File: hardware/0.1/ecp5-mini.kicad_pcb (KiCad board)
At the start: 4 copper layers, 52 x 27 mm, 105 parts, among them J1 Micro_SD_Card, J2 JTAG, J3 S7 Mini, J4 S7 Mini, J5 USB_C_Receptacle_USB2.0, Q1 BSS138, Q2 BSS138, Q3 BSS138, Q4 BSS138, SW1 KMR2, U1 ECP5U_12_CABGA256, U2 TLV73325PDBV, U3 TLV62568DBV, U4 USBLC6-2P6, U5 TLV62568DBV, U6 W25Q128JVPIQ, U7 S27KL0641, X1 DSC6101CI2A-016

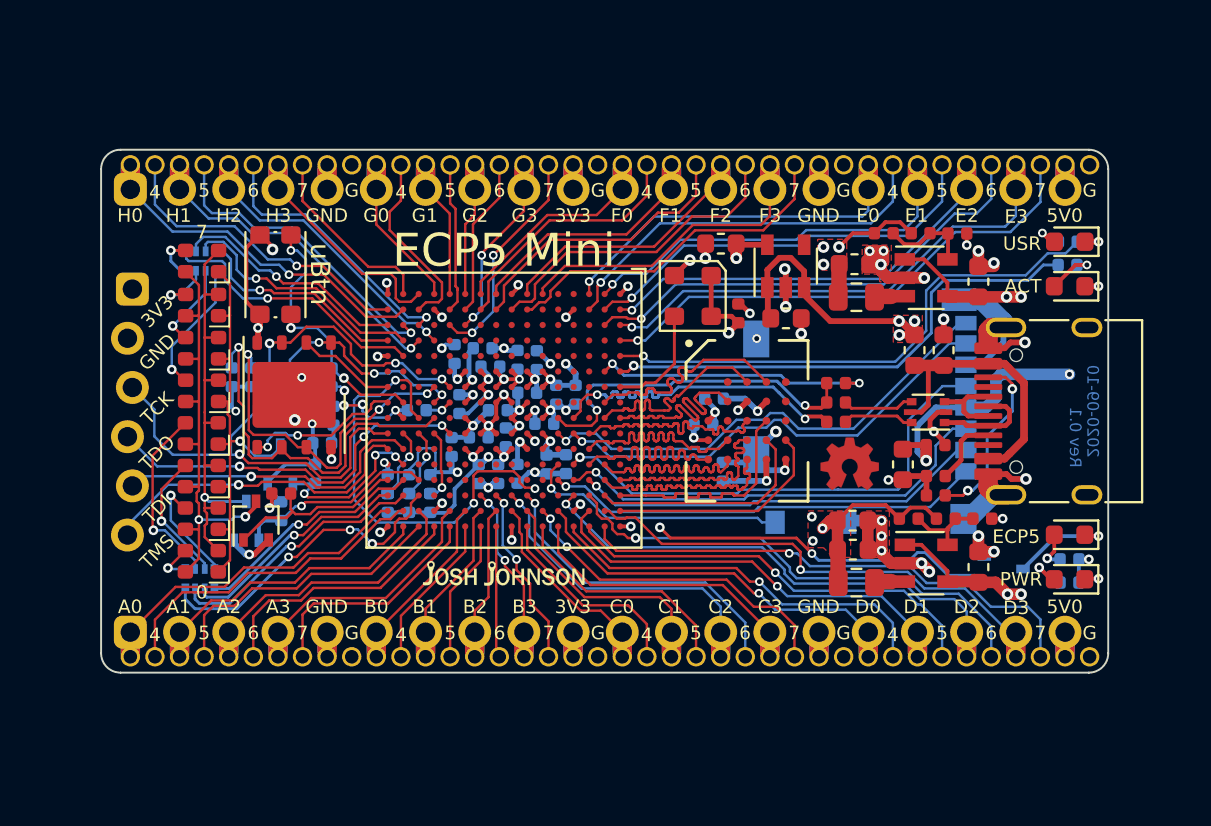
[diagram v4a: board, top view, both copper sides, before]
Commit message: add fiducals
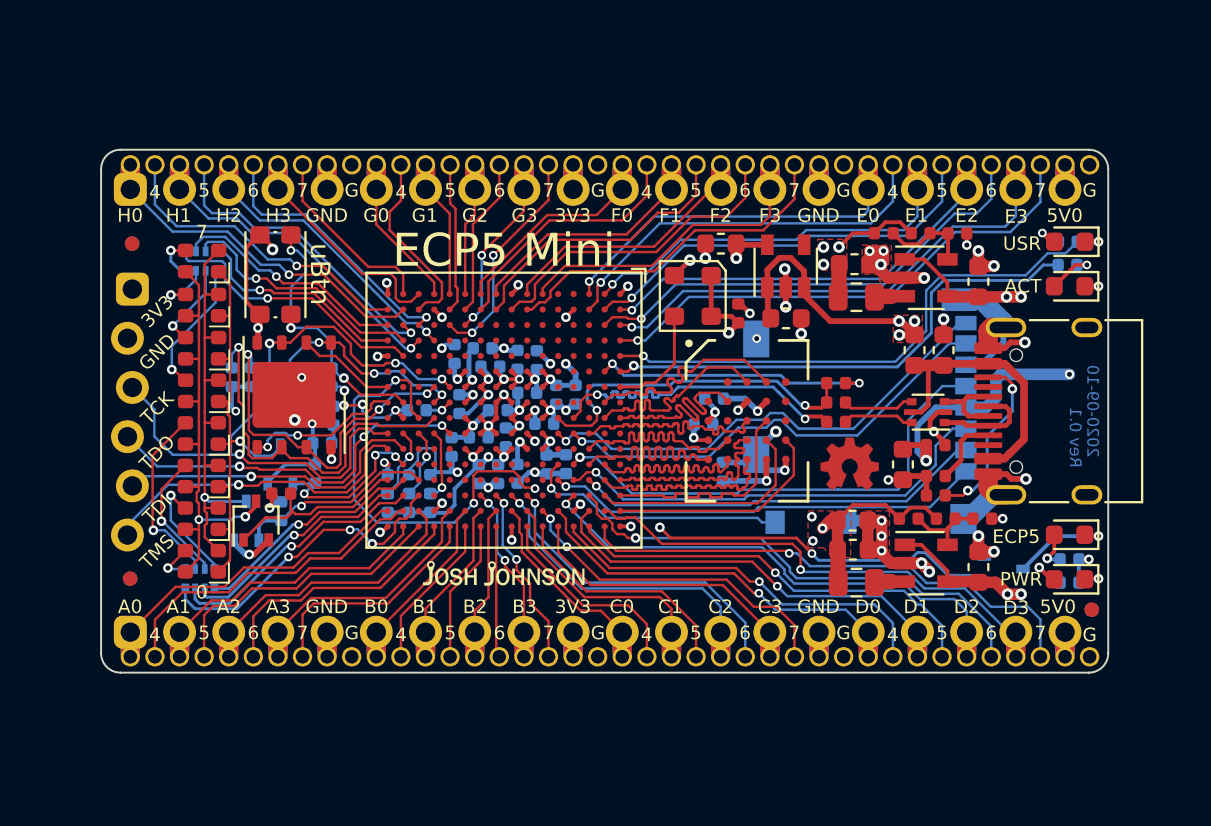
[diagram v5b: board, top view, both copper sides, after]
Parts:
- added FID1: Fiducial, Fiducial:Fiducial_0.75mm_Mask1.5mm, F.Cu at (147.3, 105.2)
- added FID2: Fiducial, Fiducial:Fiducial_0.75mm_Mask1.5mm, B.Cu at (97.8, 86.3)
- added FID3: Fiducial, Fiducial:Fiducial_0.75mm_Mask1.5mm, B.Cu at (147.3, 105.2)
- added FID4: Fiducial, Fiducial:Fiducial_0.75mm_Mask1.5mm, B.Cu at (97.7, 103.6)
- added FID5: Fiducial, Fiducial:Fiducial_0.75mm_Mask1.5mm, F.Cu at (97.8, 86.3)
- added FID6: Fiducial, Fiducial:Fiducial_0.75mm_Mask1.5mm, F.Cu at (97.7, 103.6)
- U6: value W25Q128JVPIQ -> W25Q128JVPIM
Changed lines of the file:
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@@
     )
   )
+  (module "Fiducial:Fiducial_0.75mm_Mask1.5mm" (layer "F.Cu")
+    (at 97.8 86.3)
+    (descr "Circular Fiducial, 0.75mm bare copper, 1.5mm soldermask opening (Level B)")
+    (tags "fiducial")
+    (property "Sheet file" "/mnt/530683E96DD773A1/Dropbox/Projects/ecp5-mini/hardware/0.1/ecp5-mini.kicad_sch")
+    (property "Sheet name" "")
+    (attr smd)
+    (fp_text reference "FID5" (at 0 -2) (layer "F.SilkS") hide
+      (effects (font (size 1 1) (thickness 0.15)))
+    )
+    (fp_text value "Fiducial" (at 0 2) (layer "F.Fab")
+      (effects (font (size 1 1) (thickness 0.15)))
+    )
+    (fp_text user "${REFERENCE}" (at 0 0) (layer "F.Fab") hide
+      (effects (font (size 0.3 0.3) (thickness 0.05)))
+    )
+    (fp_circle (center 0 0) (end 1 0) (layer "F.CrtYd") (width 0.05))
+    (fp_circle (center 0 0) (end 0.75 0) (layer "F.Fab") (width 0.1))
+    (pad "" smd circle (at 0 0) (size 0.75 0.75) (layers "F.Cu" "F.Mask")
+      (solder_mask_margin 0.375) (clearance 0.375))
+  )
   (module "Resistor_SMD:R_0402_1005Metric" (layer "F.Cu")
     (at 139.3 98.3 180)
@@
     )
   )
+  (module "Fiducial:Fiducial_0.75mm_Mask1.5mm" (layer "F.Cu")
+    (at 147.35 105.2)
+    (descr "Circular Fiducial, 0.75mm bare copper, 1.5mm soldermask opening (Level B)")
+    (tags "fiducial")
+    (property "Sheet file" "/mnt/530683E96DD773A1/Dropbox/Projects/ecp5-mini/hardware/0.1/ecp5-mini.kicad_sch")
+    (property "Sheet name" "")
+    (attr smd)
+    (fp_text reference "FID1" (at 0 -2) (layer "F.SilkS") hide
+      (effects (font (size 1 1) (thickness 0.15)))
+    )
+    (fp_text value "Fiducial" (at 0 2) (layer "F.Fab")
+      (effects (font (size 1 1) (thickness 0.15)))
+    )
+    (fp_text user "${REFERENCE}" (at 0 0) (layer "F.Fab") hide
+      (effects (font (size 0.3 0.3) (thickness 0.05)))
+    )
+    (fp_circle (center 0 0) (end 1 0) (layer "F.CrtYd") (width 0.05))
+    (fp_circle (center 0 0) (end 0.75 0) (layer "F.Fab") (width 0.1))
+    (pad "" smd circle (at 0 0) (size 0.75 0.75) (layers "F.Cu" "F.Mask")
+      (solder_mask_margin 0.375) (clearance 0.375))
+  )
   (module "josh-led:LED_TRI_2020" (layer "F.Cu")
     (at 101.415 89.474 180)
@@
     (descr "Oscilator suits Microchip DSC 6xxx series")
     (property "MPN" "DSC6101CI2A-016.0000 ")
+    (property "Manufacturer" "Microchip")
     (property "Mouser" "579-101CI2A0160000 ")
     (property "Sheet file" "/mnt/530683E96DD773A1/Dropbox/Projects/ecp5-mini/hardware/0.1/ecp5-mini.kicad_sch")
@@
     )
   )
+  (module "Fiducial:Fiducial_0.75mm_Mask1.5mm" (layer "F.Cu")
+    (at 97.7 103.6)
+    (descr "Circular Fiducial, 0.75mm bare copper, 1.5mm soldermask opening (Level B)")
+    (tags "fiducial")
+    (property "Sheet file" "/mnt/530683E96DD773A1/Dropbox/Projects/ecp5-mini/hardware/0.1/ecp5-mini.kicad_sch")
+    (property "Sheet name" "")
+    (attr smd)
+    (fp_text reference "FID6" (at 0 -2) (layer "F.SilkS") hide
+      (effects (font (size 1 1) (thickness 0.15)))
+    )
+    (fp_text value "Fiducial" (at 0 2) (layer "F.Fab")
+      (effects (font (size 1 1) (thickness 0.15)))
+    )
+    (fp_text user "${REFERENCE}" (at 0 0) (layer "F.Fab") hide
+      (effects (font (size 0.3 0.3) (thickness 0.05)))
+    )
+    (fp_circle (center 0 0) (end 1 0) (layer "F.CrtYd") (width 0.05))
+    (fp_circle (center 0 0) (end 0.75 0) (layer "F.Fab") (width 0.1))
+    (pad "" smd circle (at 0 0) (size 0.75 0.75) (layers "F.Cu" "F.Mask")
+      (solder_mask_margin 0.375) (clearance 0.375))
+  )
   (module "Capacitor_SMD:C_0402_1005Metric" (layer "F.Cu")
     (at 129.1 89.9 90)
@@
       (effects (font (size 1 1) (thickness 0.15)))
     )
-    (fp_text value "W25Q128JVPIQ" (at 0 3.45 -90) (layer "F.Fab")
+    (fp_text value "W25Q128JVPIM" (at 0 3.45 -90) (layer "F.Fab")
       (effects (font (size 1 1) (thickness 0.15)))
     )
@@
     )
   )
+  (module "Fiducial:Fiducial_0.75mm_Mask1.5mm" (layer "B.Cu")
+    (at 97.8 86.3 180)
+    (descr "Circular Fiducial, 0.75mm bare copper, 1.5mm soldermask opening (Level B)")
+    (tags "fiducial")
+    (property "Sheet file" "/mnt/530683E96DD773A1/Dropbox/Projects/ecp5-mini/hardware/0.1/ecp5-mini.kicad_sch")
+    (property "Sheet name" "")
+    (attr smd)
+    (fp_text reference "FID2" (at 0 2) (layer "B.SilkS") hide
+      (effects (font (size 1 1) (thickness 0.15)) (justify mirror))
+    )
+    (fp_text value "Fiducial" (at 0 -2) (layer "B.Fab")
+      (effects (font (size 1 1) (thickness 0.15)) (justify mirror))
+    )
+    (fp_text user "${REFERENCE}" (at 0 0) (layer "B.Fab") hide
+      (effects (font (size 0.3 0.3) (thickness 0.05)) (justify mirror))
+    )
+    (fp_circle (center 0 0) (end 1 0) (layer "B.CrtYd") (width 0.05))
+    (fp_circle (center 0 0) (end 0.75 0) (layer "B.Fab") (width 0.1))
+    (pad "" smd circle (at 0 0 180) (size 0.75 0.75) (layers "B.Cu" "B.Mask")
+      (solder_mask_margin 0.375) (clearance 0.375))
+  )
   (module "Resistor_SMD:R_0402_1005Metric" (layer "B.Cu")
     (at 104.95 93.2 90)
@@
     )
   )
+  (module "Fiducial:Fiducial_0.75mm_Mask1.5mm" (layer "B.Cu")
+    (at 147.35 105.2 180)
+    (descr "Circular Fiducial, 0.75mm bare copper, 1.5mm soldermask opening (Level B)")
+    (tags "fiducial")
+    (property "Sheet file" "/mnt/530683E96DD773A1/Dropbox/Projects/ecp5-mini/hardware/0.1/ecp5-mini.kicad_sch")
+    (property "Sheet name" "")
+    (attr smd)
+    (fp_text reference "FID3" (at 0 2) (layer "B.SilkS") hide
+      (effects (font (size 1 1) (thickness 0.15)) (justify mirror))
+    )
+    (fp_text value "Fiducial" (at 0 -2) (layer "B.Fab")
+      (effects (font (size 1 1) (thickness 0.15)) (justify mirror))
+    )
+    (fp_text user "${REFERENCE}" (at 0 0) (layer "B.Fab") hide
+      (effects (font (size 0.3 0.3) (thickness 0.05)) (justify mirror))
+    )
+    (fp_circle (center 0 0) (end 1 0) (layer "B.CrtYd") (width 0.05))
+    (fp_circle (center 0 0) (end 0.75 0) (layer "B.Fab") (width 0.1))
+    (pad "" smd circle (at 0 0 180) (size 0.75 0.75) (layers "B.Cu" "B.Mask")
+      (solder_mask_margin 0.375) (clearance 0.375))
+  )
   (module "Capacitor_SMD:C_0402_1005Metric" (layer "B.Cu")
     (at 116.685 94.9)
@@
     )
   )
+  (module "Fiducial:Fiducial_0.75mm_Mask1.5mm" (layer "B.Cu")
+    (at 97.7 103.6 180)
+    (descr "Circular Fiducial, 0.75mm bare copper, 1.5mm soldermask opening (Level B)")
+    (tags "fiducial")
+    (property "Sheet file" "/mnt/530683E96DD773A1/Dropbox/Projects/ecp5-mini/hardware/0.1/ecp5-mini.kicad_sch")
+    (property "Sheet name" "")
+    (attr smd)
+    (fp_text reference "FID4" (at 0 2) (layer "B.SilkS") hide
+      (effects (font (size 1 1) (thickness 0.15)) (justify mirror))
+    )
+    (fp_text value "Fiducial" (at 0 -2) (layer "B.Fab")
+      (effects (font (size 1 1) (thickness 0.15)) (justify mirror))
+    )
+    (fp_text user "${REFERENCE}" (at 0 0) (layer "B.Fab") hide
+      (effects (font (size 0.3 0.3) (thickness 0.05)) (justify mirror))
+    )
+    (fp_circle (center 0 0) (end 1 0) (layer "B.CrtYd") (width 0.05))
+    (fp_circle (center 0 0) (end 0.75 0) (layer "B.Fab") (width 0.1))
+    (pad "" smd circle (at 0 0 180) (size 0.75 0.75) (layers "B.Cu" "B.Mask")
+      (solder_mask_margin 0.375) (clearance 0.375))
+  )
   (module "Capacitor_SMD:C_0402_1005Metric" (layer "B.Cu")
     (at 107.615 96.6 180)
@@
     (effects (font (size 0.6 0.6) (thickness 0.127)) (justify mirror))
   )
-  (gr_text "G" (at 147.24 106.4) (layer "F.SilkS")
+  (gr_text "G" (at 147.24 106.5) (layer "F.SilkS")
     (effects (font (size 0.7 0.7) (thickness 0.12)))
   )
@@
     (effects (font (size 0.7 0.7) (thickness 0.12)))
   )
-  (gr_text "5V0" (at 145.95 105.05) (layer "F.SilkS")
+  (gr_text "5V0" (at 145.6 105.05) (layer "F.SilkS")
     (effects (font (size 0.7 0.7) (thickness 0.12)))
   )
@@
   (segment (start 135.81 84.59) (end 135.5 84.9) (width 0.127) (layer "B.Cu") (net 60))
   (segment (start 103.7 86.5) (end 104.35 85.85) (width 0.2) (layer "F.Cu") (net 61))
+  (segment (start 142.275 87.475) (end 142.3 87.45) (width 0.6) (layer "F.Cu") (net 61))
   (segment (start 117.8 94.9) (end 117.4 95.3) (width 0.2) (layer "F.Cu") (net 61))
   (segment (start 135.897636 86.675) (end 135.885136 86.6875) (width 0.6) (layer "F.Cu") (net 61))
@@
   (segment (start 116.6 94.49192) (end 116.999999 94.091921) (width 0.2) (layer "F.Cu") (net 61))
   (segment (start 117.4 95.3) (end 117.8 95.7) (width 0.2) (layer "F.Cu") (net 61))
-  (segment (start 141.497636 87.475) (end 142.297636 87.475) (width 0.6) (layer "F.Cu") (net 61))
   (segment (start 131.551499 97.949991) (end 131.50149 98) (width 0.3) (layer "F.Cu") (net 61))
   (segment (start 146.9875 88.5) (end 147.7 88.5) (width 0.3) (layer "F.Cu") (net 61))
@@
   (segment (start 125.8 87.95) (end 126.6 87.15) (width 0.25) (layer "F.Cu") (net 61))
   (segment (start 132.35 90.15625) (end 132.35 90.95) (width 0.3) (layer "F.Cu") (net 61))
+  (segment (start 141.497636 87.475) (end 142.275 87.475) (width 0.6) (layer "F.Cu") (net 61))
   (segment (start 116.6 95.3) (end 116.6 94.5) (width 0.2) (layer "F.Cu") (net 61))
   (segment (start 136.597636 86.675) (end 136.597636 87.241755) (width 0.6) (layer "F.Cu") (net 61))
@@
   (via (at 106.2 95.4) (size 0.6) (drill 0.3) (layers "F.Cu" "B.Cu") (net 61))
   (via (at 106.561897 93.205247) (size 0.45) (drill 0.25) (layers "F.Cu" "B.Cu") (net 61))
-  (via (at 142.297636 87.3) (size 0.6) (drill 0.3) (layers "F.Cu" "B.Cu") (net 61))
+  (via (at 142.297636 87.45) (size 0.6) (drill 0.3) (layers "F.Cu" "B.Cu") (net 61))
   (via (at 117.8 94.9) (size 0.5) (drill 0.25) (layers "F.Cu" "B.Cu") (net 61))
   (via (at 110.949992 88.322256) (size 0.5) (drill 0.25) (layers "F.Cu" "B.Cu") (net 61))

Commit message: set clearances to a more reasonable number
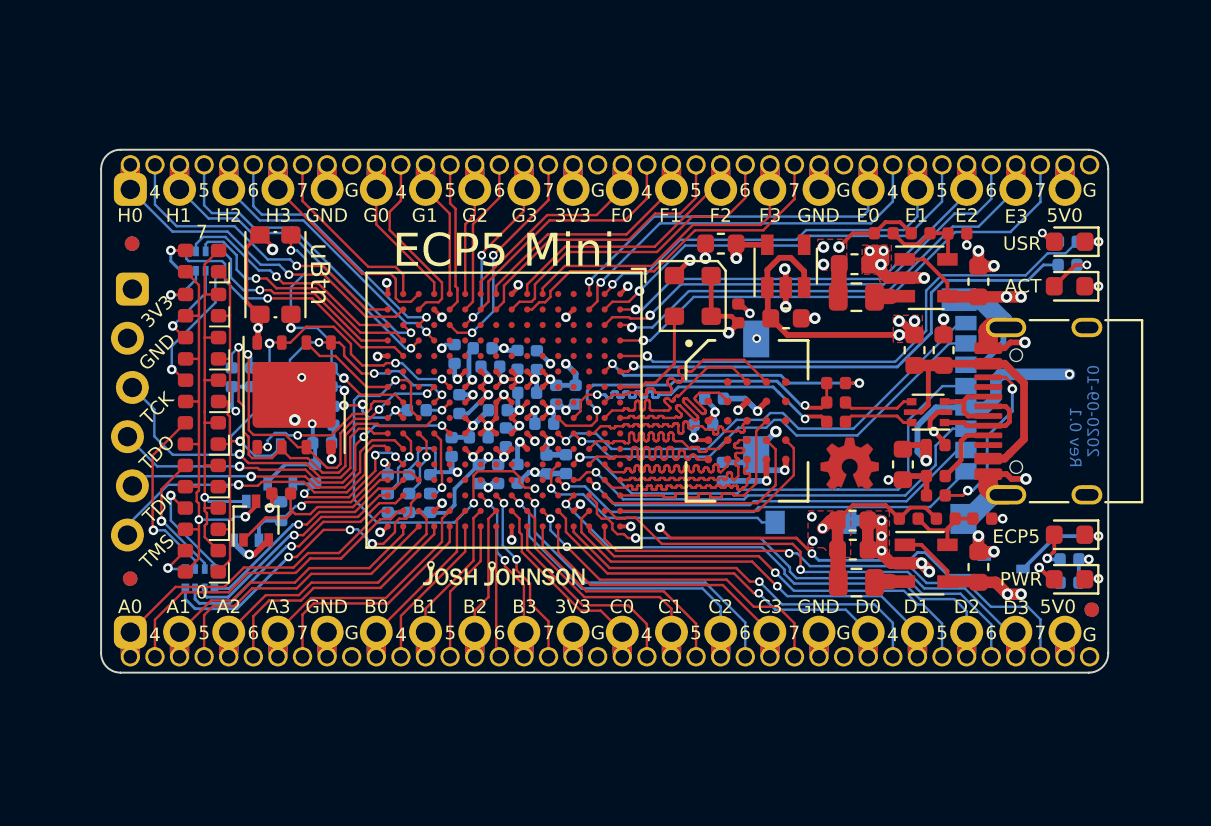
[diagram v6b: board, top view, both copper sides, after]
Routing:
- net +5V: track 71.6 -> 73.8 mm
- net /PORT_E3: track 24.2 -> 23.4 mm

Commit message: quad pmod looks good
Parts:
- U6: value W25Q128JVPIM -> W25Q128JVPIQ
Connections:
- net /FPGA_OK renamed /LED_ACT
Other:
- board text added: "2020-09-13"
- board text removed: "2020-09-10"
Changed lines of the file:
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@@
       (usegerberextensions true)
       (usegerberattributes false)
-      (usegerberadvancedattributes true)
+      (usegerberadvancedattributes false)
       (creategerberjobfile false)
       (svguseinch false)
@@
   (net 229 "/PORT_H0")
   (net 230 "/LED_USR")
-  (net 231 "/FPGA_OK")
+  (net 231 "/LED_ACT")
   (net 232 "Net-(U1-PadR7)")
   (net 233 "Net-(U1-PadR6)")
@@
     (descr "Circular Fiducial, 0.75mm bare copper, 1.5mm soldermask opening (Level B)")
     (tags "fiducial")
+    (property "DNP" "DNP")
     (property "Sheet file" "/mnt/530683E96DD773A1/Dropbox/Projects/ecp5-mini/hardware/0.1/ecp5-mini.kicad_sch")
     (property "Sheet name" "")
@@
     (descr "Circular Fiducial, 0.75mm bare copper, 1.5mm soldermask opening (Level B)")
     (tags "fiducial")
+    (property "DNP" "DNP")
     (property "Sheet file" "/mnt/530683E96DD773A1/Dropbox/Projects/ecp5-mini/hardware/0.1/ecp5-mini.kicad_sch")
     (property "Sheet name" "")
@@
       (net 230 "/LED_USR") (pinfunction "PT18A/+"))
     (pad "A6" smd circle (at -2 -6 270) (size 0.32 0.32) (layers "F.Cu" "F.Paste" "F.Mask")
-      (net 231 "/FPGA_OK") (pinfunction "PT18B/-"))
+      (net 231 "/LED_ACT") (pinfunction "PT18B/-"))
     (pad "A7" smd circle (at -1.2 -6 270) (size 0.32 0.32) (layers "F.Cu" "F.Paste" "F.Mask")
       (net 167 "/CLK_16MHZ") (pinfunction "PT29A/+/PCLKT0_0"))
@@
     (descr "Circular Fiducial, 0.75mm bare copper, 1.5mm soldermask opening (Level B)")
     (tags "fiducial")
+    (property "DNP" "DNP")
     (property "Sheet file" "/mnt/530683E96DD773A1/Dropbox/Projects/ecp5-mini/hardware/0.1/ecp5-mini.kicad_sch")
     (property "Sheet name" "")
@@
     (descr "WSON, 8 Pin (http://www.winbond.com/resource-files/w25q32jv%20revg%2003272018%20plus.pdf (page 68)), generated with kicad-footprint-generator ipc_dfn_qfn_generator.py")
     (tags "WSON DFN_QFN")
-    (property "MPN" "W25Q128JVPIM")
+    (property "MPN" "W25Q128JVPIQ")
     (property "Manufacturer" "Winbond")
-    (property "Mouser" "454-W25Q128JVPIM")
+    (property "Mouser" "454-W25Q128JVPIQ")
     (property "Sheet file" "fpga-config.kicad_sch")
     (property "Sheet name" "FPGA Config")
@@
       (effects (font (size 1 1) (thickness 0.15)))
     )
-    (fp_text value "W25Q128JVPIM" (at 0 3.45 -90) (layer "F.Fab")
+    (fp_text value "W25Q128JVPIQ" (at 0 3.45 -90) (layer "F.Fab")
       (effects (font (size 1 1) (thickness 0.15)))
     )
@@
     (descr "Circular Fiducial, 0.75mm bare copper, 1.5mm soldermask opening (Level B)")
     (tags "fiducial")
+    (property "DNP" "DNP")
     (property "Sheet file" "/mnt/530683E96DD773A1/Dropbox/Projects/ecp5-mini/hardware/0.1/ecp5-mini.kicad_sch")
     (property "Sheet name" "")
@@
     (descr "Circular Fiducial, 0.75mm bare copper, 1.5mm soldermask opening (Level B)")
     (tags "fiducial")
+    (property "DNP" "DNP")
     (property "Sheet file" "/mnt/530683E96DD773A1/Dropbox/Projects/ecp5-mini/hardware/0.1/ecp5-mini.kicad_sch")
     (property "Sheet name" "")
@@
     (descr "Circular Fiducial, 0.75mm bare copper, 1.5mm soldermask opening (Level B)")
     (tags "fiducial")
+    (property "DNP" "DNP")
     (property "Sheet file" "/mnt/530683E96DD773A1/Dropbox/Projects/ecp5-mini/hardware/0.1/ecp5-mini.kicad_sch")
     (property "Sheet name" "")
@@
     (fp_line (start -0.5 0.25) (end 0.5 0.25) (layer "B.Fab") (width 0.1))
     (pad "1" smd roundrect (at -0.485 0) (size 0.59 0.64) (layers "B.Cu" "B.Paste" "B.Mask") (roundrect_rratio 0.25)
-      (net 231 "/FPGA_OK"))
+      (net 231 "/LED_ACT"))
     (pad "2" smd roundrect (at 0.485 0) (size 0.59 0.64) (layers "B.Cu" "B.Paste" "B.Mask") (roundrect_rratio 0.25)
       (net 166 "Net-(D12-Pad2)"))
@@
     (effects (font (size 0.6 0.6) (thickness 0.127)) (justify mirror))
   )
-  (gr_text "2020-09-10" (at 147.4 94.95 270) (layer "B.Cu")
+  (gr_text "2020-09-13" (at 147.4 94.95 270) (layer "B.Cu")
     (effects (font (size 0.6 0.6) (thickness 0.127)) (justify mirror))
   )
@@
     (effects (font (size 0.7 0.7) (thickness 0.12)))
   )
-  (gr_text "2020-09-10" (at 147.4 94.95 270) (layer "B.Mask")
+  (gr_text "2020-09-13" (at 147.4 94.95 270) (layer "B.Mask")
     (effects (font (size 0.6 0.6) (thickness 0.127)) (justify mirror))
   )
